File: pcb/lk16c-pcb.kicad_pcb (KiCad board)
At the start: 2 copper layers, 76.2 x 76.2 mm, 48 parts, among them J1 Conn_01x03, J2 Conn_01x04, J3 Conn_01x04, J5 Conn_01x04, J6 Conn_01x04, J7 Conn_01x04, J8 Conn_01x04, J9 Conn_01x04, SW1 SW_Push, SW10 SW_Push, SW11 SW_Push, SW12 SW_Push, SW13 SW_Push, SW14 SW_Push, SW15 SW_Push, SW16 SW_Push, SW17 SW_Push, SW2 SW_Push, SW3 SW_Push, SW4 SW_Push, SW5 SW_Push, SW6 SW_Push, SW7 SW_Push, SW8 SW_Push, SW9 SW_Push, U1 RaspberryPi_Pico

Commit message: Update board to board connector
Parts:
- J1: renamed from J3; footprint LKBD_Connector:PinHeader_1x04_THT_P2.54mm_nSilk -> LKBD_Connector:EdgeConnector_1x04_THT_P2.54mm_Right_nSilk
- J2: footprint LKBD_Connector:PinHeader_1x04_THT_P2.54mm_nSilk -> LKBD_Connector:EdgeConnector_1x04_THT_P2.54mm_Left_nSilk
- J3: renamed from J5; footprint LKBD_Connector:PinHeader_1x04_THT_P2.54mm_nSilk -> LKBD_Connector:EdgeConnector_1x04_THT_P2.54mm_Right_nSilk
- J4: renamed from J7; footprint LKBD_Connector:PinHeader_1x04_THT_P2.54mm_nSilk -> LKBD_Connector:EdgeConnector_1x04_THT_P2.54mm_Left_nSilk
- J5: renamed from J6; footprint LKBD_Connector:PinHeader_1x04_THT_P2.54mm_nSilk -> LKBD_Connector:EdgeConnector_1x04_THT_P2.54mm_Right_nSilk
- J6: renamed from J8; footprint LKBD_Connector:PinHeader_1x04_THT_P2.54mm_nSilk -> LKBD_Connector:EdgeConnector_1x04_THT_P2.54mm_Left_nSilk
- renumbered J1 to J7, J9 to J8

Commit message: Update PCB from Schematic
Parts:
- J1, J3, J5: footprint LKBD_Connector:EdgeConnector_1x04_THT_P2.54mm_Right_nSilk -> Connector:EdgeHeader_1x04_THT_P2.54mm_Right
- J2, J4, J6: footprint LKBD_Connector:EdgeConnector_1x04_THT_P2.54mm_Left_nSilk -> Connector:EdgeHeader_1x04_THT_P2.54mm_Left
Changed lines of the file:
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@@
 		)
 	)
-	(footprint "LKBD_Connector:EdgeConnector_1x04_THT_P2.54mm_Left_nSilk"
+	(footprint "Connector:EdgeHeader_1x04_THT_P2.54mm_Left"
 		(layer "B.Cu")
 		(at 103.505 60.325 180)
@@
 		)
 	)
-	(footprint "LKBD_Connector:EdgeConnector_1x04_THT_P2.54mm_Right_nSilk"
+	(footprint "Connector:EdgeHeader_1x04_THT_P2.54mm_Right"
 		(layer "B.Cu")
 		(at 29.845 41.275 180)
@@
 		)
 	)
-	(footprint "LKBD_Connector:EdgeConnector_1x04_THT_P2.54mm_Left_nSilk"
+	(footprint "Connector:EdgeHeader_1x04_THT_P2.54mm_Left"
 		(layer "B.Cu")
 		(at 103.505 79.375 180)
@@
 		)
 	)
-	(footprint "LKBD_Connector:EdgeConnector_1x04_THT_P2.54mm_Right_nSilk"
+	(footprint "Connector:EdgeHeader_1x04_THT_P2.54mm_Right"
 		(layer "B.Cu")
 		(at 29.845 60.325 180)
@@
 		)
 	)
-	(footprint "LKBD_Connector:EdgeConnector_1x04_THT_P2.54mm_Right_nSilk"
+	(footprint "Connector:EdgeHeader_1x04_THT_P2.54mm_Right"
 		(layer "B.Cu")
 		(at 29.845 79.375 180)
@@
 		)
 	)
-	(footprint "LKBD_Connector:EdgeConnector_1x04_THT_P2.54mm_Left_nSilk"
+	(footprint "Connector:EdgeHeader_1x04_THT_P2.54mm_Left"
 		(layer "B.Cu")
 		(at 103.505 41.275 180)

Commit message: Update LKBD and move edge connectors to leave space for an LED stirp
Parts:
- J7: value Conn_01x03 -> PINHD_1x03_ARGB
- J8: value Conn_01x04 -> PINHD_1x05_I2C; footprint LKBD_Connector:PinHeader_1x04_THT_P2.54mm_nSilk -> LKBD_Connector:PinHeader_1x05_THT_P2.54mm_nSilk
- moved J1 1.27 mm to (29.8, 40.0)
- moved J2 1.27 mm to (103.5, 40.0)
- moved J5 1.27 mm to (29.8, 80.6)
- moved J6 1.27 mm to (103.5, 80.6)
- moved J8 1.27 mm to (71.1, 47.6)
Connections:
- J8 pad 3: /SCL -> /SDA
- J8 pad 4: /SDA -> /SCL
- U1 pad 2: unconnected-(U1-GPIO1-Pad2) -> /IO1
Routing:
- net /IO1: track 0.00 -> 26.1 mm
- net /SDA: track 18.8 -> 15.5 mm
- net /SCL: track 15.2 -> 18.2 mm
- net /ROW3: track 189.8 -> 191.4 mm
- net /ROW4: track 202.6 -> 204.2 mm
- net /COL3: track 125.5 -> 127.1 mm
- net /COL7: track 93.3 -> 94.6 mm
- net +3.3V: track 31.9 -> 30.6 mm
- net /COL8: track 98.3 -> 99.5 mm
- net /COL6: track 88.9 -> 90.2 mm
- net /COL5: track 86.4 -> 87.6 mm
- net GND: track 31.9 -> 30.7 mm
- net /ROW2: track 161.1 -> 160.0 mm
- net /ROW1: track 80.1 -> 81.2 mm
- net /COL9: track 50.8 -> 50.2 mm
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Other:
- board text added: "IO1"

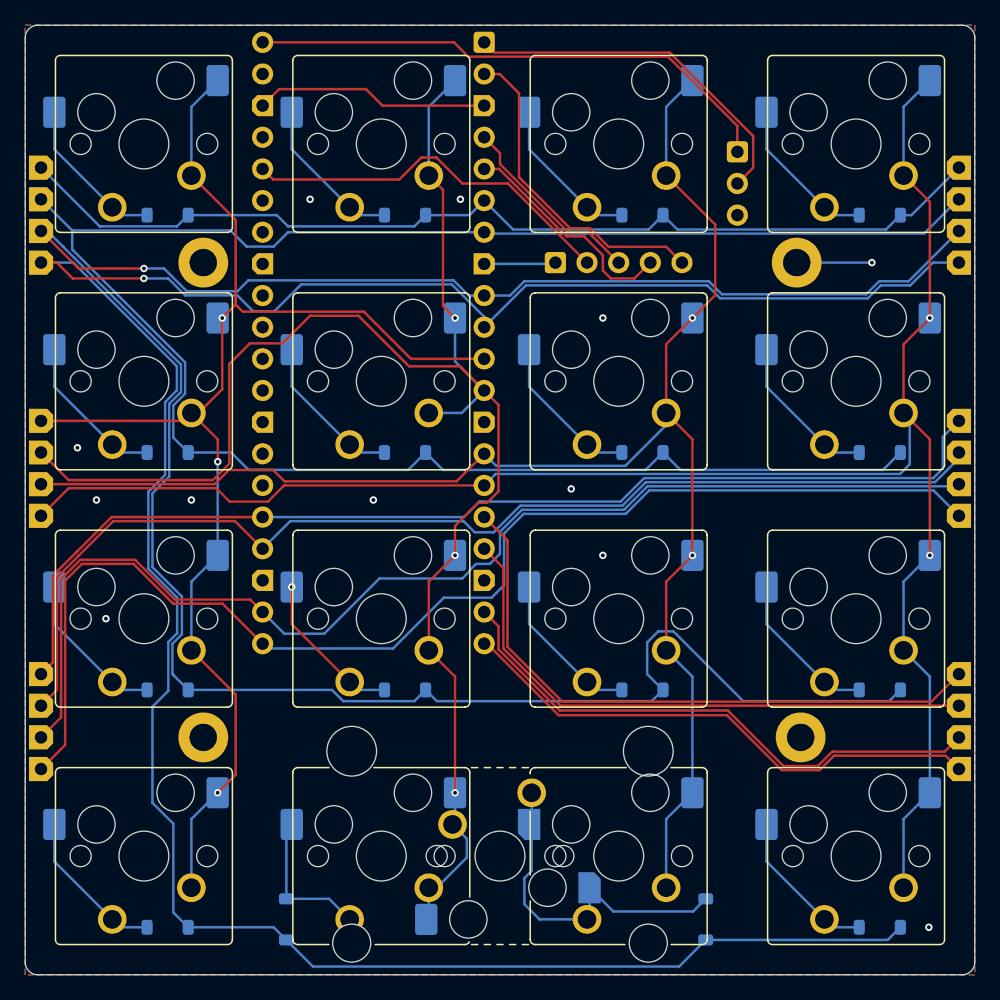
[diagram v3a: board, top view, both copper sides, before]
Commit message: Add ability to use 2× 2U Spacebars as the bottom row (#3)
* Add ability to use 2× 2U Spacebars as the bottom row
* Move Fab DataMatrix footprint
* Add plate variant for 2space
* Fix mounting hole paste
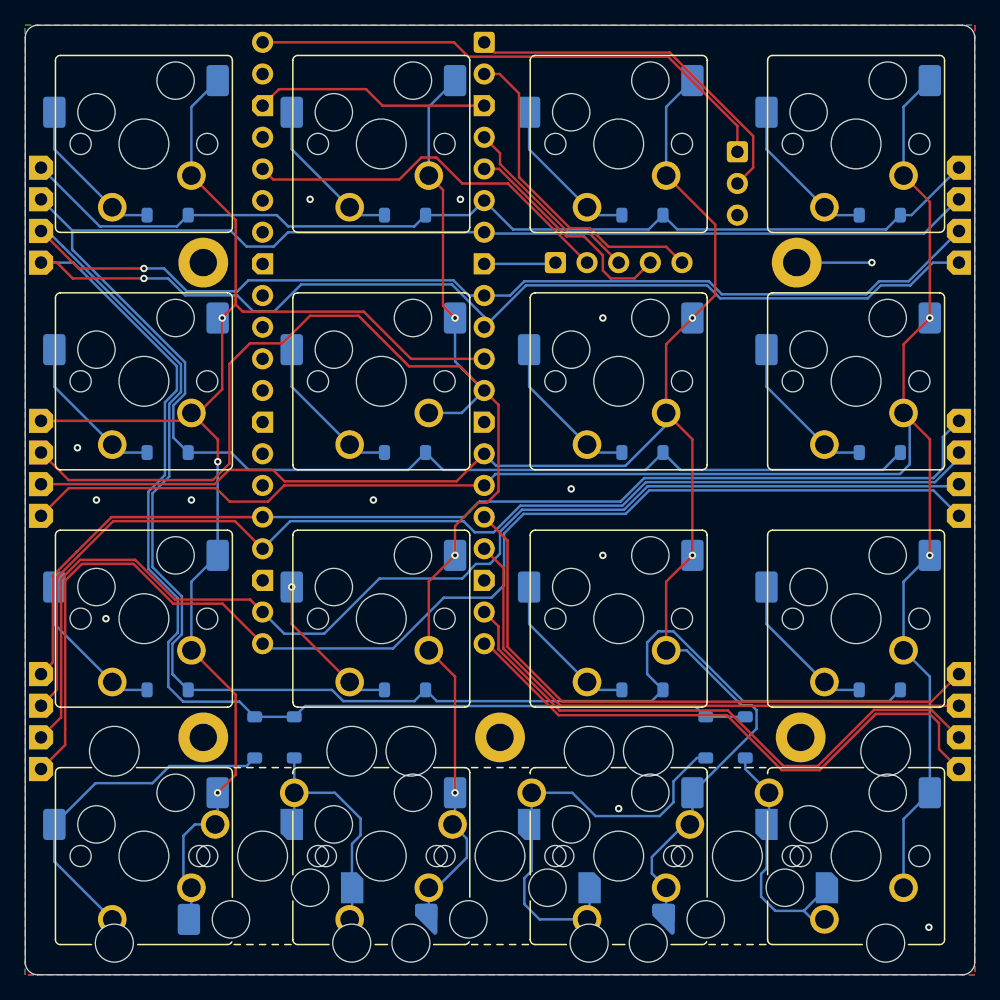
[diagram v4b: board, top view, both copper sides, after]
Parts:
- added H5: MountingHole_Pad, LKBD_MountingHole:MountingHole_M2, F.Cu at (66.7, 85.7)
- added S14: MX_stab, LKBD_StabMX:Stabilizer_MX_2U, F.Cu at (47.6, 95.2)
- added S18: MX_stab, LKBD_StabMX:Stabilizer_MX_2U, F.Cu at (85.7, 95.2)
- added SW14: SW_Push, LKBD_KeySwitch:SW_MX_Slim_HotSwap_THT_sqSilk, B.Cu at (47.6, 95.2)
- added SW18: SW_Push, LKBD_KeySwitch:SW_MX_Slim_HotSwap_THT_sqSilk, B.Cu at (85.7, 95.2)
- moved TXT1 21.7 mm to (85.7, 78.7)
- moved D19 18.7 mm to (86.4, 85.7), turned to -90 degrees
- moved D13 16.8 mm to (47.0, 85.7), turned to -90 degrees
- moved D15 14.6 mm to (50.2, 85.7), turned to -90 degrees
- moved D17 14.6 mm to (83.2, 85.7), turned to -90 degrees
- renumbered D14 to D15, D16 to D17, D17 to D19, S15 to S16, SW14 to SW15, SW15 to SW16, SW16 to SW17, SW17 to SW19
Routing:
- net /ROW4: track 204.2 -> 171.4 mm
- net Net-(D13-A): track 12.6 -> 28.7 mm
- net /COL3: track 127.1 -> 136.6 mm
- net Net-(D15-A): track 11.9 -> 20.1 mm
- net Net-(D19-A): track 12.6 -> 20.7 mm
- net Net-(D17-A): track 28.0 -> 35.2 mm
- net /COL1: track 107.7 -> 111.8 mm
- net /COL12: track 43.2 -> 47.2 mm
- net /COL11: track 45.3 -> 47.1 mm
- net GND: vias 12 -> 13

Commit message: Bump version to v1.01
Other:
- board text added: "v1.01"
- board text removed: "v1.00"
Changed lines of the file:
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@@
 		)
 	)
-	(gr_text "v1.00"
+	(gr_text "v1.01"
 		(at 81.825 66.275 0)
 		(layer "B.SilkS")
